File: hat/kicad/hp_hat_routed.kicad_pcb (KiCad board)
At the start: 4 copper layers, 99.9 x 17.8 mm, 54 parts, among them J1 Hand-soldered cable (3 wires), J3 Nano solder-stack header, J4 Nano solder-stack header, Q1 AO3400A, Q2 AO3400A, U4 INA226

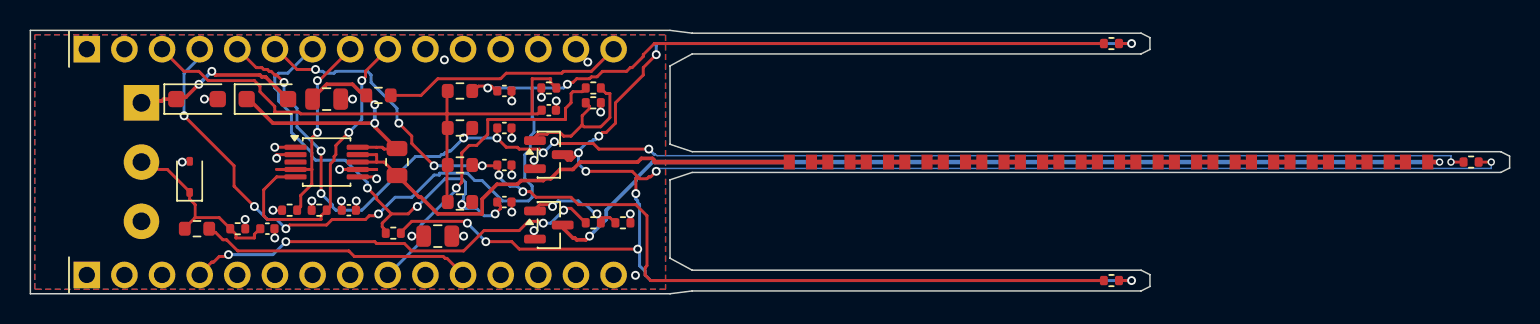
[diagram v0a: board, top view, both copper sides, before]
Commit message: Update flat-nano and hat to the reviewed designs; refresh the website
Boards (both at the Arduino Nano R4 outline, 43.18 x 17.78 mm):
- Hand-routed copper (preroute.py) replaces the auto-router; release.py
  rebuilds, checks (ERC, DRC all severities, parity, Kelvin, solder vias,
  layout quality) and exports the order files with a release manifest.
- Layout quality gate: power copper >= 0.5 mm outer / 1.2 mm inner,
  heat sources on the center line, mirrored side needles, left/right
  copper within 10% on every layer.
- flat-nano: 5 V buck regulator (LMR36503), single-sided assembly,
  cable solder holes, programming-clip holes. Hat: parts on both faces,
  Nano pins kept.
- R11 330 ohm -> 1.5 kohm so pin D4 stays within the RA4M1 4 mA limit.
- TH1 is the right needle and TH3 the left, as seen on the top face with
  the cable end up (pin map unchanged: A2 = TH1, A0 = TH3).
- No revision labels; old-version checksums and auto-router reports
  removed.

Website (docs/) and twin:
- Board data, drawing, current-flow lines, tags, parts list, guided tour
  and model match the current flat-nano.
- Plainer wording for the C3/C4 filtering explanations.

Co-Authored-By: Claude Opus 5.5 <noreply@anthropic.com>
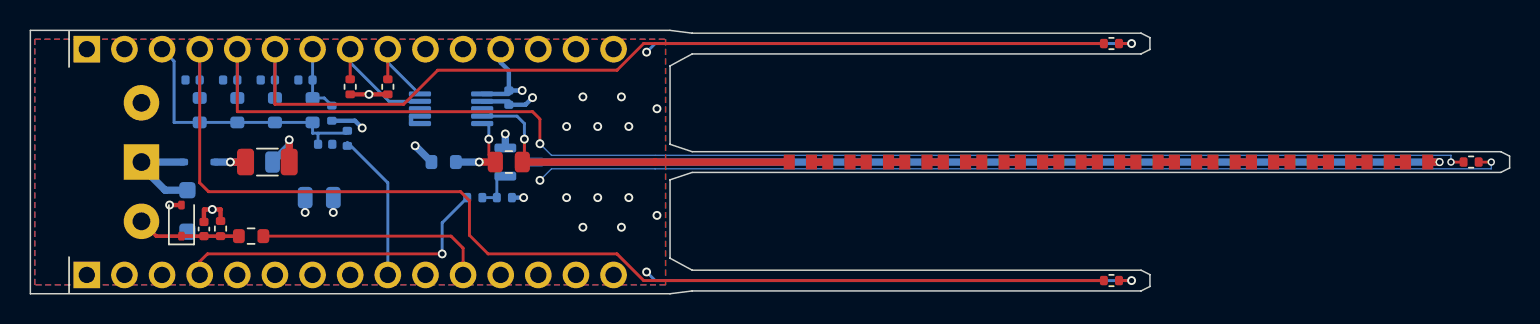
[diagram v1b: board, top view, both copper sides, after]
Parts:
- removed C2: 10u 10V, Capacitor_SMD:C_0805_2012Metric
- removed Q2: AO3400A, Package_TO_SOT_SMD:SOT-23
- removed R12: 1.5k, Resistor_SMD:R_0402_1005Metric
- removed R17: 100k, Resistor_SMD:R_0402_1005Metric
- added C17: 10u 25V, Capacitor_SMD:C_0805_2012Metric, B.Cu at (119.5, 82.4)
- added C3: 22u 25V, Capacitor_SMD:C_1206_3216Metric, F.Cu at (116.0, 80.0)
- C1, C12, C13, C21, C22, C23, C24, D2, Q1, R10, R18, R21, R22, R23, R24, R9, TH4, U4: moved to B.Cu
- D1: value 1A 40V Schottky (SOD-123F) -> 1A 40V Schottky (SOD-323); footprint Diode_SMD:D_SOD-123F -> Diode_SMD:D_SOD-323; moved to B.Cu
- J1: footprint hp_sensor:CablePads_1x03_P4mm -> hp_sensor:CableSolder_1x03
- R11: value 10 -> 1.5k; moved to B.Cu
- moved C23 21.8 mm to (111.0, 74.5), turned to 180 degrees
- moved C22 18.8 mm to (113.5, 74.5), turned to 180 degrees
- moved R23 18.0 mm to (111.4, 76.5), turned to 90 degrees
- moved C21 16.0 mm to (116.0, 74.5), turned to 180 degrees
- moved C24 15.8 mm to (118.6, 74.5), turned to 180 degrees
- moved C13 15.3 mm to (119.9, 78.8)
- moved R22 15.1 mm to (114.0, 76.5), turned to 90 degrees
- moved R11 14.0 mm to (121.4, 78.4), turned to 90 degrees
- moved C12 13.2 mm to (132.3, 75.7), turned to -90 degrees
- moved R21 12.6 mm to (116.5, 76.5), turned to 90 degrees
- moved R24 11.7 mm to (119.0, 76.5), turned to 90 degrees
- moved R7 9.53 mm to (124.1, 74.9), turned to 90 degrees
- moved R6 9.28 mm to (121.6, 74.9), turned to 90 degrees
- moved U4 9.14 mm to (128.4, 76.4)
- moved TH4 9.10 mm to (120.3, 76.7), turned to -90 degrees
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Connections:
- C21 pad 1: A0_TH1 -> A2_TH1
- C23 pad 1: A2_TH3 -> A0_TH3
- J4 pad 4: A0_TH1 -> A0_TH3
- J4 pad 6: A2_TH3 -> A2_TH1
- R11 pad 1: +5V -> D4_EXC
- R21 pad 2: A0_TH1 -> A2_TH1
- R23 pad 2: A2_TH3 -> A0_TH3
- TH1 pad 1: A0_TH1 -> A2_TH1
- TH1 pad 2: TH_RTN -> GND
- TH2 pad 2: TH_RTN -> GND
- TH3 pad 1: A2_TH3 -> A0_TH3
- TH3 pad 2: TH_RTN -> GND
- TH4 pad 2: TH_RTN -> GND
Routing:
- net TH_RTN: track 167.5 -> 0.00 mm, vias 12 -> 0
- net GND: track 17.7 -> 149.6 mm, vias 22 -> 26
- net A0_TH1: track 87.9 -> 0.00 mm, vias 6 -> 0
- net A0_TH3: track 0.00 -> 77.5 mm
- net A2_TH3: track 67.3 -> 0.00 mm, vias 6 -> 0
- net A2_TH1: track 0.00 -> 64.7 mm
- net A3_TH4: track 30.9 -> 4.81 mm, vias 4 -> 0
- net VREF: track 40.2 -> 18.5 mm
- net A5_SCL: track 21.6 -> 5.93 mm, vias 2 -> 0
- net D4_EXC: track 21.9 -> 10.1 mm, vias 1 -> 0
- net HEAT_P: track 34.7 -> 23.7 mm, vias 0 -> 1
- net EXC_GATE: track 10.4 -> 0.00 mm
- net A4_SDA: track 16.1 -> 8.73 mm, vias 2 -> 0
- net D9_HEAT: track 29.1 -> 22.0 mm, vias 4 -> 1
- net VIN: track 11.6 -> 5.76 mm, vias 2 -> 0
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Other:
- board text removed: "NANO FACES IN"
- board text removed: "USB"

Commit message: Prefer JLC Basic/Preferred parts and fewer BOM lines; wider primer page
Flat-nano 27 -> 25 BOM lines (13 -> 9 Extended), hat 21 -> 20 (10 -> 6):
- Schottky diodes: 1N5819WS C191023 (Basic, same SOD-323)
- C1 and C17: one 10 uF 50 V 0805 part, C440198 (Basic)
- all 100 nF: the 50 V part C307331 (Basic)
- C4 3.3 nF: C26404 (Preferred); SMF16CA/SMF15CA TVS: C19077511/C19077510 (Preferred)
Copper and placement unchanged (all tracks, vias and positions identical); full
release checks pass. Twin parts data, flat-nano README and primer Appendix A
updated to match.

Primer page: wider column, larger text and more space between sections on
screen; print layout unchanged.

Co-Authored-By: Claude Opus 5.5 <noreply@anthropic.com>
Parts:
- C1: value 4.7u 50V -> 10u 50V
- C17: value 10u 25V -> 10u 50V
